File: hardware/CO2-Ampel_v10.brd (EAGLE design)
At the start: 50 x 50 mm, 69 parts, among them IC1 VREG-AP2111H-3V3, IC2 ATSAMD21G18A-MU, IC3 ATWINC1500-MR210PB, IC33 IN-S63DTLS, IC34 SCD30, IC7 ATECC608A-MAHDA, J1 USB-C-S, J2 JST4, J5 JST4, SW1 PTS645SH50SMTR92-Grey, SW2 PTS645SK50SMTR92-Red, T1 N-Chn, X1 PASSER-07, X2 PASSER-07, X3 PASSER-07, X4 PASSER-07

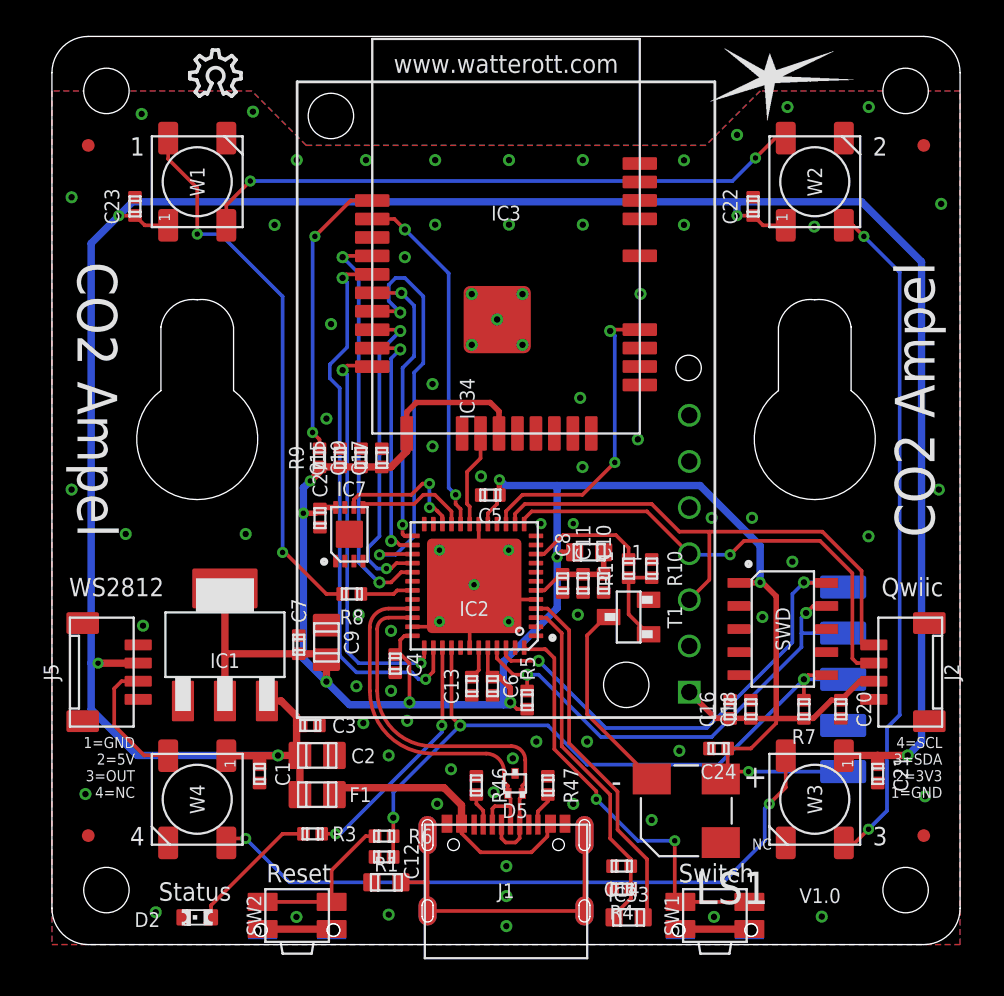
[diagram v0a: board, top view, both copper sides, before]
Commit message: updated schematics
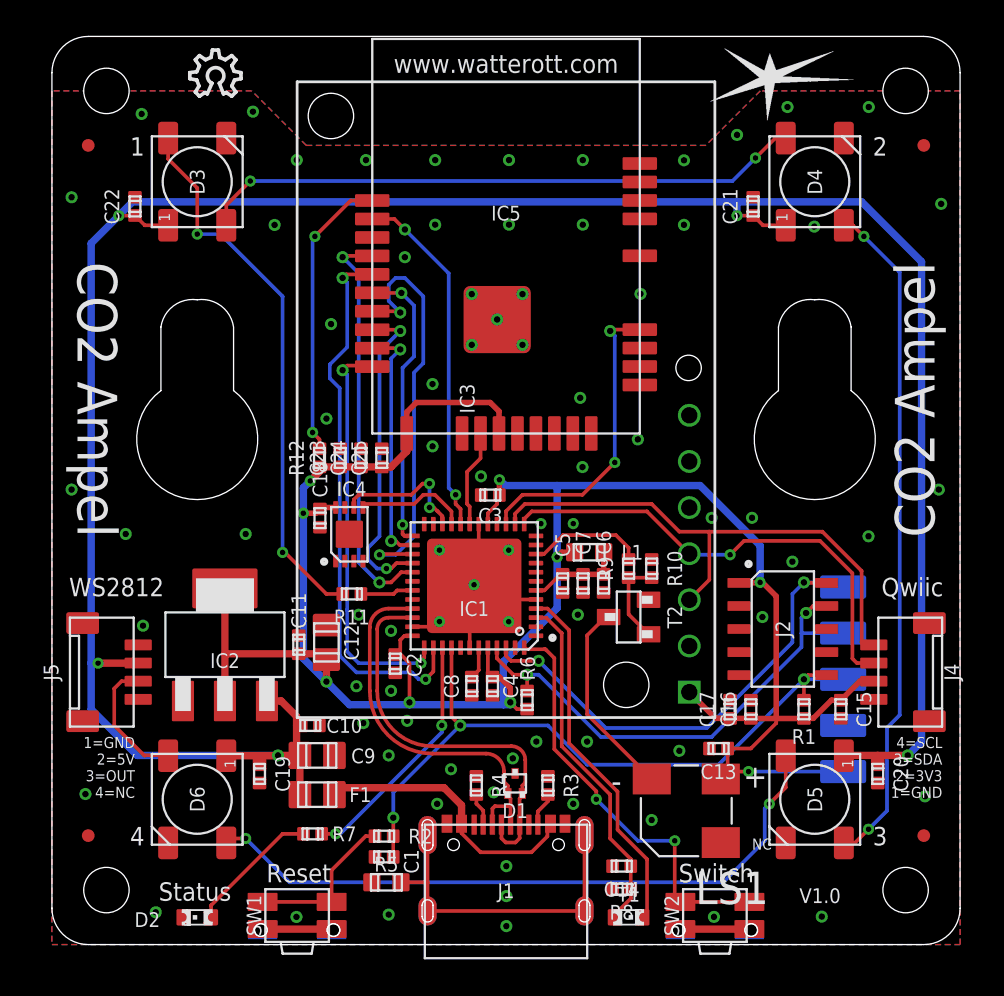
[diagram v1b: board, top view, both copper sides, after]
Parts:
- removed C27: 100n, we-rcl:C0402
- removed IC33: IN-S63DTLS, we-sensor:C0603
- removed IC34: SCD30, we-sensor:SCD30
- removed LOGO7: LOGO_CE-4, we-symbol:CE_4MM
- removed R46, R47: 5k1, we-rcl:C0402
- removed SWD: SWD-2X5-SMD, we-board:SWD-2X5_SMD
- removed W3: WS2812B, we-opto:WS2812B
- added C25: 100n, we-rcl:C0402
- added D1: D_ESD5V3U2U-03F, we-rcl:SOT723
- added IC5: ATWINC1500-MR210PB, we-chip:ATWINC1500-MX210
- added J4: JST4, we-con:JST_SM04B-SRSS-TB
- added LOGO1: LOGO_SPARK-4, we-symbol:SPARK_4MM
- added R12: 100k, we-rcl:C0402
- added R2: 330, we-rcl:C0402
- added T2: N-Chn, we-transistor:SOT23
- C10, C13, C15, C18, C19: value 2u2 -> 100n
- C12: value 100n -> 22u; device we-rcl:C0402 -> we-rcl:C0805
- C16, C23, C24, C5, C6: value 100n -> 2u2
- C2: value 22u -> 100n; device we-rcl:C0805 -> we-rcl:C0402
- D5: value D_ESD5V3U2U-03F -> WS2812B; device we-rcl:SOT723 -> we-opto:WS2812B
- IC1: value VREG-AP2111H-3V3 -> ATSAMD21G18A-MU; device we-power:SOT223 -> we-chip:QFN48-PAD
- IC2: value ATSAMD21G18A-MU -> VREG-AP2111H-3V3; device we-chip:QFN48-PAD -> we-power:SOT223
- IC3: value ATWINC1500-MR210PB -> SCD30; device we-chip:ATWINC1500-MX210 -> we-sensor:SCD30
- J2: value JST4 -> SWD-2X5-SMD; device we-con:JST_SM04B-SRSS-TB -> we-board:SWD-2X5_SMD
- LOGO4: value LOGO_SPARK-4 -> LOGO_ROHS-4; device we-symbol:SPARK_4MM -> we-symbol:ROHS_4MM
- LOGO5: value LOGO_ROHS-4 -> LOGO_CE-4; device we-symbol:ROHS_4MM -> we-symbol:CE_4MM
- R1: value 0 -> 10k; device we-rcl:C0603 -> we-rcl:C0402
- R11: value 100 -> 330
- R3: value 1k -> 5k1
- R4: value 100k -> 5k1
- R5: value 1k -> 0; device we-rcl:C0402 -> we-rcl:C0603
- R6: value 330 -> 1k
- R7: value 10k -> 1k
- R8: value 330 -> 100k
- R9: value 100k -> 100
- SW1: value PTS645SH50SMTR92-Grey -> PTS645SK50SMTR92-Red
- SW2: value PTS645SK50SMTR92-Red -> PTS645SH50SMTR92-Grey
- T1: value N-Chn -> PT-IN-S63DTLS; device we-transistor:SOT23 -> we-opto@1:C0603T
- moved X2 59.7 mm to (48.0, 6.00), turned to 0 degrees
- moved X3 59.7 mm to (2.00, 6.00)
- moved LOGO4 46.1 mm to (9.04, 13.1), flipped to the bottom
- moved X1 38.0 mm to (2.00, 44.0), turned to 90 degrees
- moved X4 38.0 mm to (48.0, 44.0)
- moved C22 34.0 mm to (4.57, 40.6)
- moved C21 32.0 mm to (38.6, 40.6), turned to 0 degrees
- moved C15 30.8 mm to (43.4, 13.0), turned to 180 degrees
- moved R7 27.9 mm to (14.4, 6.10), turned to 270 degrees
- moved C18 26.0 mm to (14.8, 23.5), turned to 180 degrees
- moved C24 25.4 mm to (17.0, 26.8), turned to 0 degrees
- moved R1 24.9 mm to (41.4, 13.0), turned to 180 degrees
- moved C17 23.7 mm to (37.3, 13.0)
- moved SW1 23.0 mm to (13.5, 1.60)
- moved SW2 23.0 mm to (36.5, 1.60)
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- renumbered IC7 to IC4, LOGO6 to LOGO2, SWD_TP to J3, W1 to D3, W2 to D4, W4 to D6
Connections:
- net +3V3: now also C11.2, C12.2, C13.2, C2.2, C23.2, C25.2, C3.2, IC1.17, IC1.36, IC1.44, IC2.2, IC2.4, IC3.1, IC5.20, IC5.23, J2.VCC, J4.2, R1.1, R12.2, R6.1; no longer C19.2, C20.2, C27.2, C5.2, C6.2, C7.2, C9.2, IC1.2, IC1.4, IC2.17, IC2.36, IC2.44, IC3.20, IC3.23, IC34.1, J2.2, R5.1, R7.1, R9.2, SWD.VCC
- net +5V: now also C10.2, C19.2, C20.2, C9.2, D5.1, IC2.3; no longer C1.2, C2.2, C23.2, C3.2, IC1.3, W3.1
- net CC1: now also R4.1; no longer R46.1
- net CC2: now also R3.1; no longer R47.1
- net CFG: now also IC5.10, R12.1; no longer IC3.10, R9.1
- net D0_LIGHTSENS: now also IC1.3, R8.2, T1.E; no longer IC2.3, IC33.2, R4.2
- net D10_WINC_EN: now also IC1.19, IC5.22; no longer IC2.19, IC3.22
- net D11_WINC_WAKE: now also IC1.20, IC5.11; no longer IC2.20, IC3.11
- net D12_WINC_RST: now also IC1.15, IC5.4; no longer IC2.15, IC3.4
- net D13_WINC_IRQ: now also IC1.29, IC5.13; no longer IC2.29, IC3.13
- net D14_WINC_CS: now also IC1.27, IC5.16; no longer IC2.27, IC3.16
- net D15_WINC_MOSI: now also IC1.25, IC5.15; no longer IC2.25, IC3.15
- net D16_WINC_SCK: now also IC1.26, IC5.18; no longer IC2.26, IC3.18
- net D17_WINC_MISO: now also IC1.28, IC5.17; no longer IC2.28, IC3.17
- net D18_WINC_RX: now also IC1.38, IC5.14; no longer IC2.38, IC3.14
- net D19_WINC_TX: now also IC1.37, IC5.19; no longer IC2.37, IC3.19
- net D1_LIGHTSENS_PWR: now also IC1.4, T1.C; no longer IC2.4, IC33.1
- net D2_SWITCH: now also IC1.48, SW2.1, SW2.2; no longer IC2.48, SW1.1, SW1.2
- net D3_STATUSLED: now also IC1.39, R7.1; no longer IC2.39, R3.1
- net D4_BUZZER: now also IC1.10, R9.1; no longer IC2.10, R11.1
- net D5_WS2812: now also IC1.31, R11.2; no longer IC2.31, R8.2
- net D6_SDA: now also IC1.13, IC3.4, J4.3; no longer IC2.13, IC34.4, J2.3
- net D7_SCL: now also IC1.14, IC3.3, J4.4; no longer IC2.14, IC34.3, J2.4
- net D8_SDA: now also IC1.21; no longer IC2.21
- net D9_SCL: now also IC1.22; no longer IC2.22
- net GND: now also C25.1, D1.3, IC1.18, IC1.35, IC1.42, IC1.5, IC1.TP, IC2.1, IC3.2, IC5.12, IC5.28, IC5.9, IC5.GND, J2.GND@1, J2.GND@2, J2.GND@3, J4.1, R3.2, R4.2, R5.1, R8.1, T2.2; no longer C27.1, IC1.1, IC2.18, IC2.35, IC2.42, IC2.5, IC2.TP, IC3.12, IC3.28, IC3.9, IC3.GND, IC34.2, J2.1, R1.1, R4.1, R46.2, R47.2, SWD.GND@1, SWD.GND@2, SWD.GND@3, T1.2, W3.3
- net N$1: now also T2.3; no longer T1.3
- net N$2: now also R9.2, T2.1; no longer R11.2, T1.1
- net N$3: now also R7.2; no longer R3.2
- net N$4: now also R11.1; no longer R8.1
- net N$8: now also R2.2, SW1.1, SW1.2; no longer R6.2, SW2.1, SW2.2
- net RST: now also C1.2, IC1.40, J2.RST, R1.2, R2.1; no longer C12.2, IC2.40, R6.1, R7.2, SWD.RST
- net SHLD: now also R5.2; no longer R1.2
- net SWCLK: now also IC1.45, J2.SWCLK, R6.2; no longer IC2.45, R5.2, SWD.SWCLK
- net SWDIO: now also IC1.46, J2.SWDIO; no longer IC2.46, SWD.SWDIO
- net USB_N: now also D1.1, IC1.33; no longer D5.1, IC2.33
- net USB_P: now also D1.2, IC1.34; no longer D5.2, IC2.34
- net VCCANA: now also C5.2, C6.2, C7.2, IC1.6; no longer C10.2, C11.2, C8.2, IC2.6
- net VCCCORE: now also C8.2, IC1.43; no longer C13.2, IC2.43
- net W2OUT: now also D5.4; no longer W3.4
- net W3OUT: now also D5.2; no longer W3.2
